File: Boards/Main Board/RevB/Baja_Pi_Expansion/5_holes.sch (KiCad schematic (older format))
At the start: 5 parts

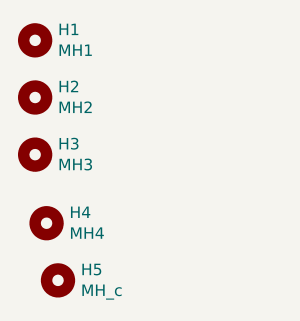
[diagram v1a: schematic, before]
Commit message: Begin to put components in place on Main-RevB
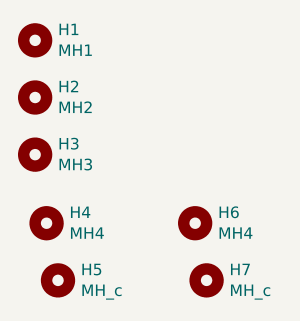
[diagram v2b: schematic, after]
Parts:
- added H6: MH4, MountingHole:MountingHole_2.7mm_M2.5, symbol Mechanical:MountingHole
- added H7: MH_c, MountingHole:MountingHole_2.7mm_M2.5, symbol Mechanical:MountingHole
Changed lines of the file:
@@
 $Descr A4 11693 8268
 encoding utf-8
-Sheet 3 2
+Sheet 2 2
 Title ""
 Date ""
@@
 	1    0    0    -1
 $EndComp
+$Comp
+L Mechanical:MountingHole H?
+U 1 1 61FDEFA3
+P 5050 3850
+AR Path="/61FDEFA3" Ref="H?"  Part="1"
+AR Path="/61664AB6/61FDEFA3" Ref="H6"  Part="1"
+F 0 "H6" H 5150 3896 50  0000 L CNN
+F 1 "MH4" H 5150 3805 50  0000 L CNN
+F 2 "MountingHole:MountingHole_2.7mm_M2.5" H 5050 3850 50  0001 C CNN
+F 3 "~" H 5050 3850 50  0001 C CNN
+	1    5050 3850
+	1    0    0    -1
+$EndComp
+$Comp
+L Mechanical:MountingHole H?
+U 1 1 61FDEFA9
+P 5100 4100
+AR Path="/61FDEFA9" Ref="H?"  Part="1"
+AR Path="/61664AB6/61FDEFA9" Ref="H7"  Part="1"
+F 0 "H7" H 5200 4146 50  0000 L CNN
+F 1 "MH_c" H 5200 4055 50  0000 L CNN
+F 2 "MountingHole:MountingHole_2.7mm_M2.5" H 5100 4100 50  0001 C CNN
+F 3 "~" H 5100 4100 50  0001 C CNN
+	1    5100 4100
+	1    0    0    -1
+$EndComp
